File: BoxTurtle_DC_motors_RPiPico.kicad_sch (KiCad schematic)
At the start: 38 parts, among them J1 Power input, J10 DC motor 1, J11 DC motor 2, J12 DC motor 3, J13 DC motor 4, J14 Screw_Terminal_01x02, J15 CAN, J2 Power input, J3 Power output, J4 Power output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

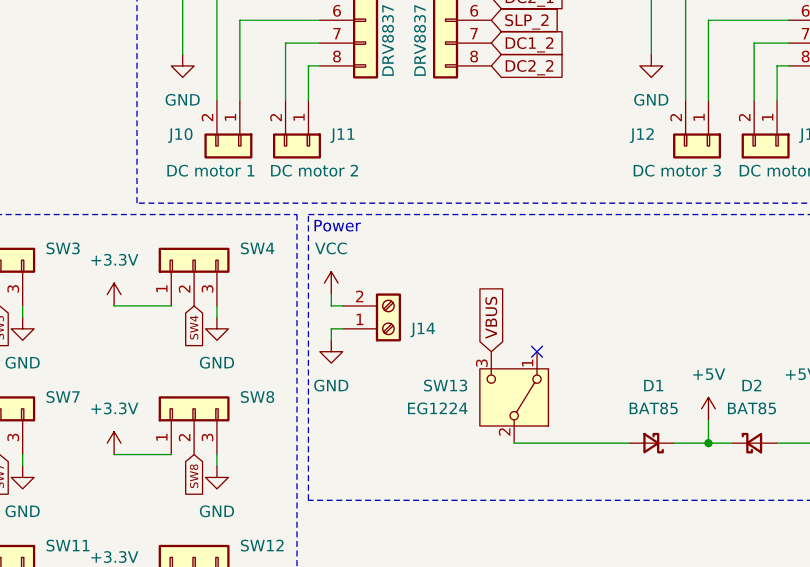
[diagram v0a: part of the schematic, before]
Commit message: Fuse & Gerber
Added the fuse for safety, also uploaded Gerber files for those who want to make their own board.
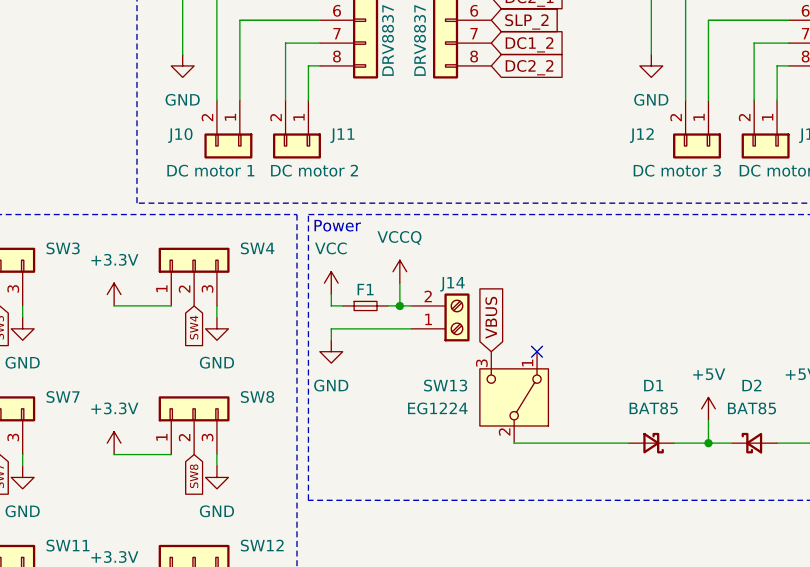
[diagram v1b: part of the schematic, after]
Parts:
- added F1: Fuse_Small, XF-506P:XF-506P, symbol Device:Fuse_Small
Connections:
- net VCC: now also F1.1; no longer J14.2 (Pin_2)
- new net VCCQ: F1.2, J14.2 (Pin_2)
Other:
- moved on the sheet: J14
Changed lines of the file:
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@@
 	)
 	(junction
+		(at 180.34 119.38)
+		(diameter 0)
+		(color 0 0 0 0)
+	)
+	(junction
 		(at 148.59 55.88)
 		(diameter 0)
@@
 	(wire
 		(pts
-			(xy 173.99 121.92) (xy 172.72 121.92)
+			(xy 172.72 121.92) (xy 181.61 121.92)
 		)
 		(stroke
@@
 	(wire
 		(pts
+			(xy 179.07 119.38) (xy 180.34 119.38)
+		)
+		(stroke
+			(width 0)
+			(type default)
+		)
+	)
+	(wire
+		(pts
 			(xy 214.63 132.08) (xy 214.63 134.62)
 		)
@@
 	(wire
 		(pts
+			(xy 180.34 116.84) (xy 180.34 119.38)
+		)
+		(stroke
+			(width 0)
+			(type default)
+		)
+	)
+	(wire
+		(pts
 			(xy 193.04 134.62) (xy 205.74 134.62)
 		)
@@
 	(wire
 		(pts
+			(xy 180.34 119.38) (xy 181.61 119.38)
+		)
+		(stroke
+			(width 0)
+			(type default)
+		)
+	)
+	(wire
+		(pts
 			(xy 138.43 119.38) (xy 138.43 120.65)
 		)
@@
 	)
 	(symbol
+		(lib_id "power:VCCQ")
+		(at 180.34 116.84 0)
+		(unit 1)
+		(exclude_from_sim no)
+		(in_bom yes)
+		(on_board yes)
+		(dnp no)
+		(fields_autoplaced yes)
+		(property "Reference" "#PWR053"
+			(at 180.34 120.65 0)
+			(effects
+				(font
+					(size 1.27 1.27)
+				)
+				(hide yes)
+			)
+		)
+		(property "Value" "VCCQ"
+			(at 180.34 111.76 0)
+			(effects
+				(font
+					(size 1.27 1.27)
+				)
+			)
+		)
+		(property "Footprint" ""
+			(at 180.34 116.84 0)
+			(effects
+				(font
+					(size 1.27 1.27)
+				)
+				(hide yes)
+			)
+		)
+		(property "Datasheet" ""
+			(at 180.34 116.84 0)
+			(effects
+				(font
+					(size 1.27 1.27)
+				)
+				(hide yes)
+			)
+		)
+		(property "Description" "Power symbol creates a global label with name \"VCCQ\""
+			(at 180.34 116.84 0)
+			(effects
+				(font
+					(size 1.27 1.27)
+				)
+				(hide yes)
+			)
+		)
+		(pin "1"
+		)
+		(instances
+			(project ""
+				(path "/1d127e4b-8316-4553-8f34-cd4a5b3a4711"
+					(reference "#PWR053")
+					(unit 1)
+				)
+			)
+		)
+	)
+	(symbol
 		(lib_id "power:GND")
 		(at 254 78.74 0)
@@
 	(symbol
 		(lib_id "Connector:Screw_Terminal_01x02")
-		(at 179.07 121.92 0)
+		(at 186.69 121.92 0)
 		(mirror x)
 		(unit 1)
@@
 		(dnp no)
 		(property "Reference" "J14"
-			(at 181.61 121.9201 0)
+			(at 184.912 116.84 0)
 			(effects
 				(font
@@
 		)
 		(property "Value" "Screw_Terminal_01x02"
-			(at 181.61 119.3801 0)
+			(at 189.23 119.3801 0)
 			(effects
 				(font
@@
 		)
 		(property "Footprint" "TerminalBlock_Phoenix:TerminalBlock_Phoenix_MKDS-3-2-5.08_1x02_P5.08mm_Horizontal"
-			(at 179.07 121.92 0)
+			(at 186.69 121.92 0)
 			(effects
 				(font
@@
 		)
 		(property "Datasheet" "~"
-			(at 179.07 121.92 0)
+			(at 186.69 121.92 0)
 			(effects
 				(font
@@
 		)
 		(property "Description" "Generic screw terminal, single row, 01x02, script generated (kicad-library-utils/schlib/autogen/connector/)"
-			(at 179.07 121.92 0)
+			(at 186.69 121.92 0)
 			(effects
 				(font
@@
 					(unit 1)
 				)
+			)
+		)
+	)
+	(symbol
+		(lib_id "Device:Fuse_Small")
+		(at 176.53 119.38 0)
+		(unit 1)
+		(exclude_from_sim no)
+		(in_bom yes)
+		(on_board yes)
+		(dnp no)
+		(property "Reference" "F1"
+			(at 176.53 117.602 0)
+			(effects
+				(font
+					(size 1.27 1.27)
+				)
+			)
+		)
+		(property "Value" "Fuse_Small"
+			(at 176.53 116.84 0)
+			(effects
+				(font
+					(size 1.27 1.27)
+				)
+				(hide yes)
+			)
+		)
+		(property "Footprint" "XF-506P:XF-506P"
+			(at 176.53 119.38 0)
+			(effects
+				(font
+					(size 1.27 1.27)
+				)
+				(hide yes)
+			)
+		)
+		(property "Datasheet" "~"
+			(at 176.53 119.38 0)
+			(effects
+				(font
+					(size 1.27 1.27)
+				)
+				(hide yes)
+			)
+		)
+		(property "Description" "Fuse, small symbol"
+			(at 176.53 119.38 0)
+			(effects
+				(font
+					(size 1.27 1.27)
+				)
+				(hide yes)
+			)
+		)
+		(pin "1"
+		)
+		(pin "2"
+		)
+		(instances
+			(project ""
+				(path "/1d127e4b-8316-4553-8f34-cd4a5b3a4711"
+					(reference "F1")
+					(unit 1)
+				)

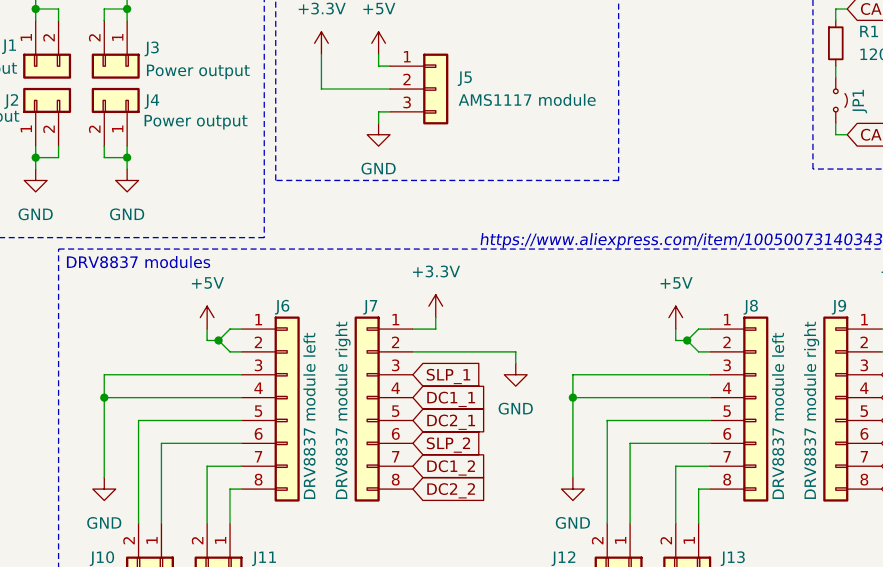
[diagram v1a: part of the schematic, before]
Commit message: Corrected 5V source for DC motors
As it was this board will blow your USB port.
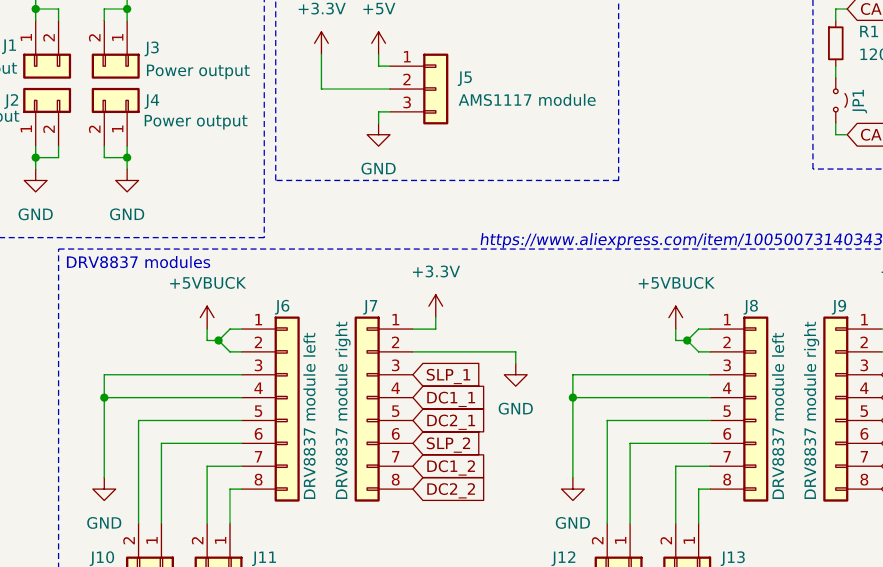
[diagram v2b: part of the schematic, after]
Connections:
- net +5V: no longer J6.1 (Pin_1), J6.2 (Pin_2), J8.1 (Pin_1), J8.2 (Pin_2)
- net +5VBUCK: now also J6.1 (Pin_1), J6.2 (Pin_2), J8.1 (Pin_1), J8.2 (Pin_2)
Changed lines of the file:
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@@
-	)
-	(symbol
-		(lib_id "power:+5V")
-		(at 219.71 74.93 0)
-		(unit 1)
-		(exclude_from_sim no)
-		(in_bom yes)
-		(on_board yes)
-		(dnp no)
-		(fields_autoplaced yes)
-		(property "Reference" "#PWR011"
-			(at 219.71 78.74 0)
-			(effects
-				(font
-					(size 1.27 1.27)
-				)
-				(hide yes)
-			)
-		)
-		(property "Value" "+5V"
-			(at 219.71 69.85 0)
-			(effects
-				(font
-					(size 1.27 1.27)
-				)
-			)
-		)
-		(property "Footprint" ""
-			(at 219.71 74.93 0)
-			(effects
-				(font
-					(size 1.27 1.27)
-				)
-				(hide yes)
-			)
-		)
-		(property "Datasheet" ""
-			(at 219.71 74.93 0)
-			(effects
-				(font
-					(size 1.27 1.27)
-				)
-				(hide yes)
-			)
-		)
-		(property "Description" "Power symbol creates a global label with name \"+5V\""
-			(at 219.71 74.93 0)
-			(effects
-				(font
-					(size 1.27 1.27)
-				)
-				(hide yes)
-			)
-		)
-		(pin "1"
-		)
-		(instances
-			(project "BoxTurtle_DC_motors_RPiPico"
-				(path "/1d127e4b-8316-4553-8f34-cd4a5b3a4711"
-					(reference "#PWR011")
-					(unit 1)
-				)
-			)
-		)
 	)
 	(symbol
@@
 	)
 	(symbol
+		(lib_id "power:+5VP")
+		(at 167.64 74.93 0)
+		(unit 1)
+		(exclude_from_sim no)
+		(in_bom yes)
+		(on_board yes)
+		(dnp no)
+		(fields_autoplaced yes)
+		(property "Reference" "#PWR054"
+			(at 167.64 78.74 0)
+			(effects
+				(font
+					(size 1.27 1.27)
+				)
+				(hide yes)
+			)
+		)
+		(property "Value" "+5VBUCK"
+			(at 167.64 69.85 0)
+			(effects
+				(font
+					(size 1.27 1.27)
+				)
+			)
+		)
+		(property "Footprint" ""
+			(at 167.64 74.93 0)
+			(effects
+				(font
+					(size 1.27 1.27)
+				)
+				(hide yes)
+			)
+		)
+		(property "Datasheet" ""
+			(at 167.64 74.93 0)
+			(effects
+				(font
+					(size 1.27 1.27)
+				)
+				(hide yes)
+			)
+		)
+		(property "Description" "Power symbol creates a global label with name \"+5VP\""
+			(at 167.64 74.93 0)
+			(effects
+				(font
+					(size 1.27 1.27)
+				)
+				(hide yes)
+			)
+		)
+		(pin "1"
+		)
+		(instances
+			(project "BoxTurtle_DC_motors_RPiPico"
+				(path "/1d127e4b-8316-4553-8f34-cd4a5b3a4711"
+					(reference "#PWR054")
+					(unit 1)
+				)
+			)
+		)
+	)
+	(symbol
 		(lib_id "Device:R_Small")
 		(at 237.49 43.18 0)
@@
 	)
 	(symbol
-		(lib_id "power:+5V")
-		(at 167.64 74.93 0)
-		(unit 1)
-		(exclude_from_sim no)
-		(in_bom yes)
-		(on_board yes)
-		(dnp no)
-		(fields_autoplaced yes)
-		(property "Reference" "#PWR010"
-			(at 167.64 78.74 0)
-			(effects
-				(font
-					(size 1.27 1.27)
-				)
-				(hide yes)
-			)
-		)
-		(property "Value" "+5V"
-			(at 167.64 69.85 0)
-			(effects
-				(font
-					(size 1.27 1.27)
-				)
-			)
-		)
-		(property "Footprint" ""
-			(at 167.64 74.93 0)
-			(effects
-				(font
-					(size 1.27 1.27)
-				)
-				(hide yes)
-			)
-		)
-		(property "Datasheet" ""
-			(at 167.64 74.93 0)
-			(effects
-				(font
-					(size 1.27 1.27)
-				)
-				(hide yes)
-			)
-		)
-		(property "Description" "Power symbol creates a global label with name \"+5V\""
-			(at 167.64 74.93 0)
-			(effects
-				(font
-					(size 1.27 1.27)
-				)
-				(hide yes)
-			)
-		)
-		(pin "1"
-		)
-		(instances
-			(project "BoxTurtle_DC_motors_RPiPico"
-				(path "/1d127e4b-8316-4553-8f34-cd4a5b3a4711"
-					(reference "#PWR010")
-					(unit 1)
-				)
-			)
-		)
-	)
-	(symbol
 		(lib_id "power:+3.3V")
 		(at 83.82 119.38 0)
@@
 					(unit 1)
 				)
+			)
+		)
+	)
+	(symbol
+		(lib_id "power:+5VP")
+		(at 219.71 74.93 0)
+		(unit 1)
+		(exclude_from_sim no)
+		(in_bom yes)
+		(on_board yes)
+		(dnp no)
+		(fields_autoplaced yes)
+		(property "Reference" "#PWR055"
+			(at 219.71 78.74 0)
+			(effects
+				(font
+					(size 1.27 1.27)
+				)
+				(hide yes)
+			)
+		)
+		(property "Value" "+5VBUCK"
+			(at 219.71 69.85 0)
+			(effects
+				(font
+					(size 1.27 1.27)
+				)
+			)
+		)
+		(property "Footprint" ""
+			(at 219.71 74.93 0)
+			(effects
+				(font
+					(size 1.27 1.27)
+				)
+				(hide yes)
+			)
+		)
+		(property "Datasheet" ""
+			(at 219.71 74.93 0)
+			(effects
+				(font
+					(size 1.27 1.27)
+				)
+				(hide yes)
+			)
+		)
+		(property "Description" "Power symbol creates a global label with name \"+5VP\""
+			(at 219.71 74.93 0)
+			(effects
+				(font
+					(size 1.27 1.27)
+				)
+				(hide yes)
+			)
+		)
+		(pin "1"
+		)
+		(instances
+			(project "BoxTurtle_DC_motors_RPiPico"
+				(path "/1d127e4b-8316-4553-8f34-cd4a5b3a4711"
+					(reference "#PWR055")
+					(unit 1)
+				)

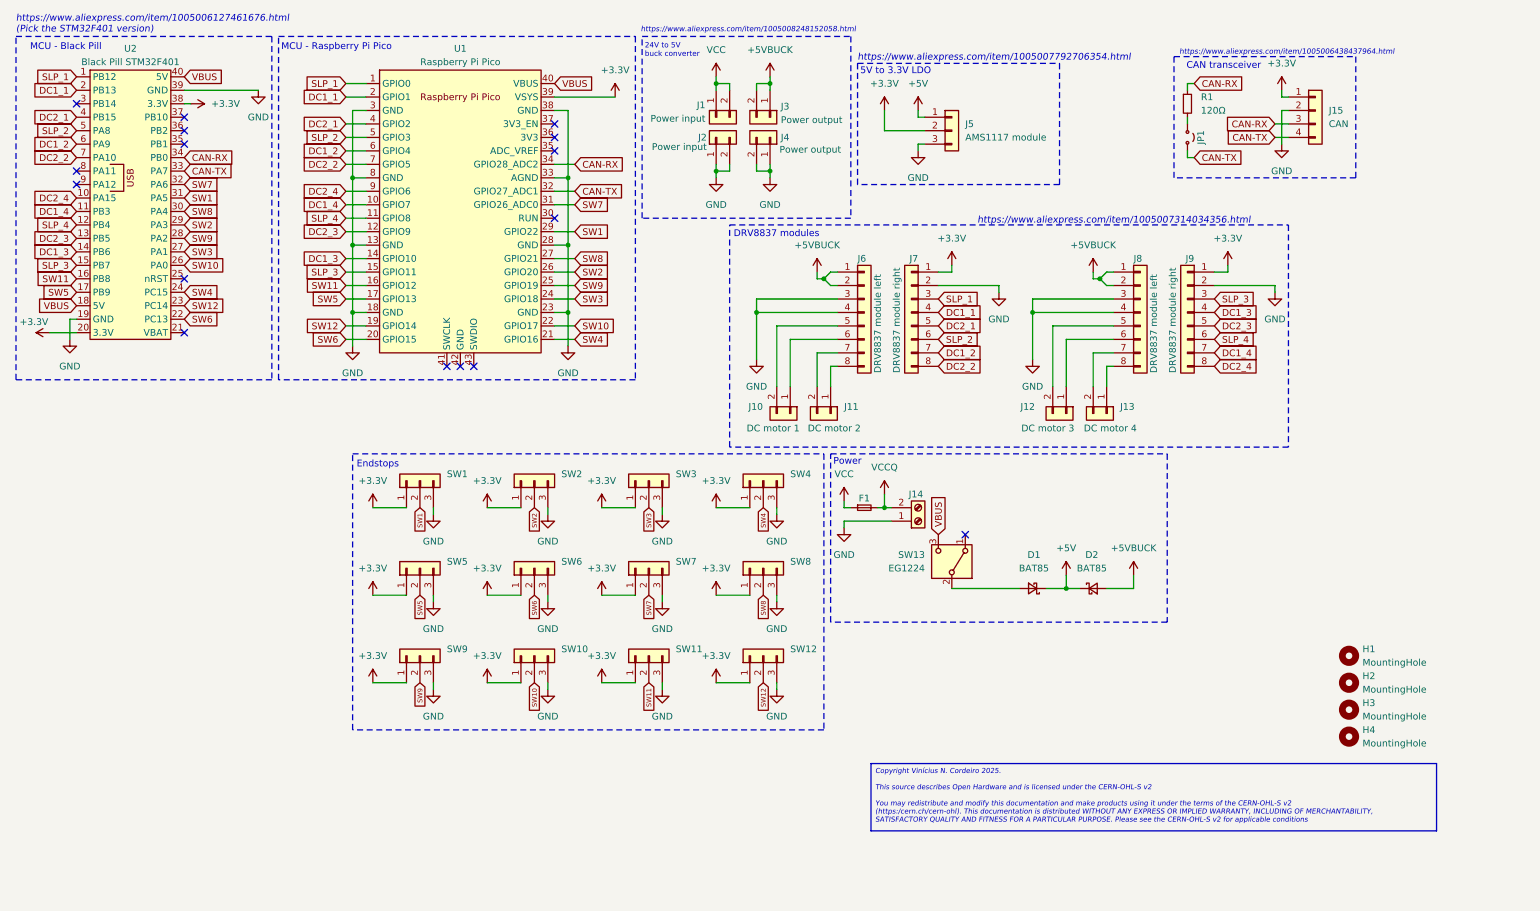
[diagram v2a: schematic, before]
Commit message: Revision 2.4 - QoL updates
Increased CAN bus resistor footprint; reduced hole diameter on Raspberry Pi Pico's socket pads for snugger fit; changed pin for SW6 on the Black Pill.
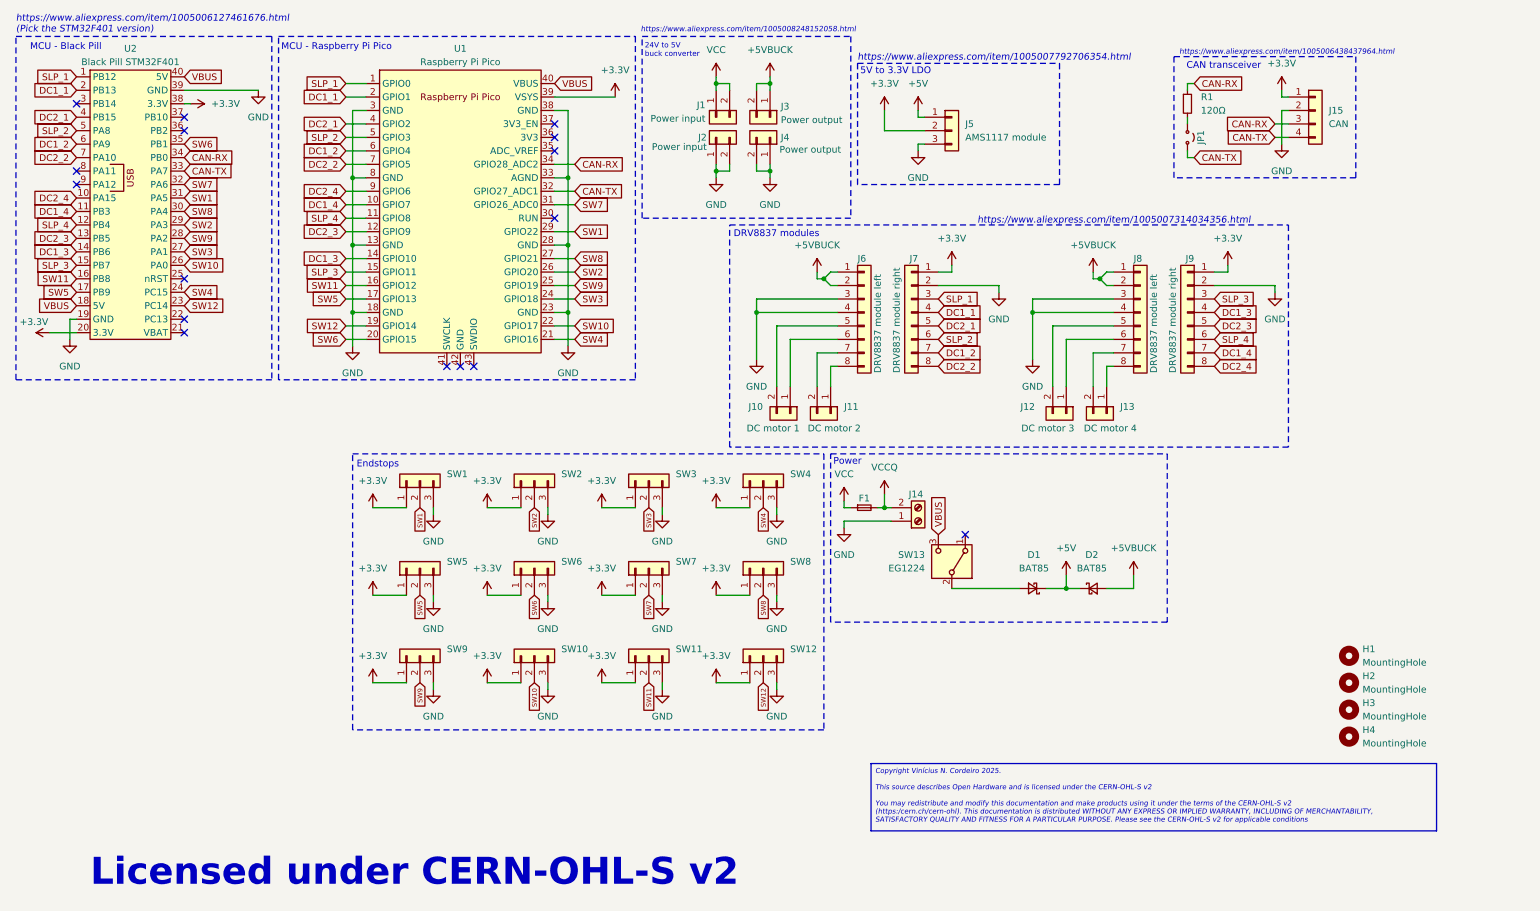
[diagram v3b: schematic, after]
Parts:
- R1: footprint Resistor_THT:R_Axial_DIN0204_L3.6mm_D1.6mm_P7.62mm_Horizontal -> Resistor_THT:R_Axial_DIN0207_L6.3mm_D2.5mm_P10.16mm_Horizontal
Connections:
- net SW6: now also U2.35 (PB1); no longer U2.22 (PC13)
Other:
- note added: "Licensed under CERN-OHL-S v2"
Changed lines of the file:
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@@
 	(title_block
 		(title "BoxTurtle DC motors standalone board")
-		(date "2025-02-03")
-		(rev "2.1")
+		(date "2025-02-22")
+		(rev "2.4")
 	)
 	(junction
@@
 	)
 	(no_connect
-		(at 48.26 50.8)
+		(at 48.26 83.82)
 	)
 	(no_connect
@@
 		)
 	)
+	(text "Licensed under CERN-OHL-S v2"
+		(exclude_from_sim no)
+		(at 91.694 188.214 0)
+		(effects
+			(font
+				(size 5.08 5.08)
+				(thickness 1.016)
+				(bold yes)
+			)
+		)
+	)
 	(text "https://www.aliexpress.com/item/1005006438437964.html"
 		(exclude_from_sim no)
@@
 	(global_label "SW6"
 		(shape input)
-		(at 48.26 83.82 0)
+		(at 48.26 50.8 0)
 		(fields_autoplaced yes)
 		(effects
@@
 		)
 		(property "Intersheetrefs" "${INTERSHEET_REFS}"
-			(at 55.1156 83.82 0)
+			(at 55.1156 50.8 0)
 			(effects
 				(font
@@
 			)
 		)
-		(property "Footprint" "Resistor_THT:R_Axial_DIN0204_L3.6mm_D1.6mm_P7.62mm_Horizontal"
+		(property "Footprint" "Resistor_THT:R_Axial_DIN0207_L6.3mm_D2.5mm_P10.16mm_Horizontal"
 			(at 237.49 43.18 0)
 			(effects

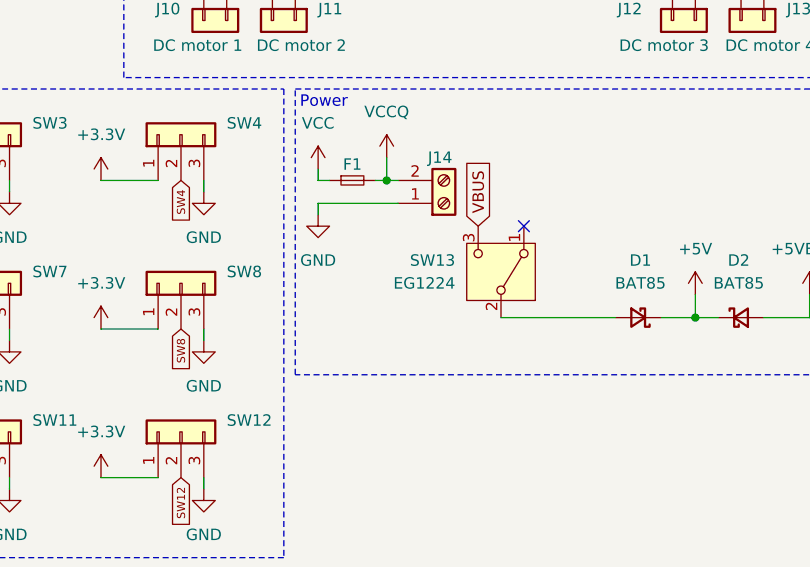
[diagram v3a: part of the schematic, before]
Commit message: Revision 2.6
Updated footprints again now that I have them on hand to accurately make measures, changed selection switch for a model that is smaller and carry more current.
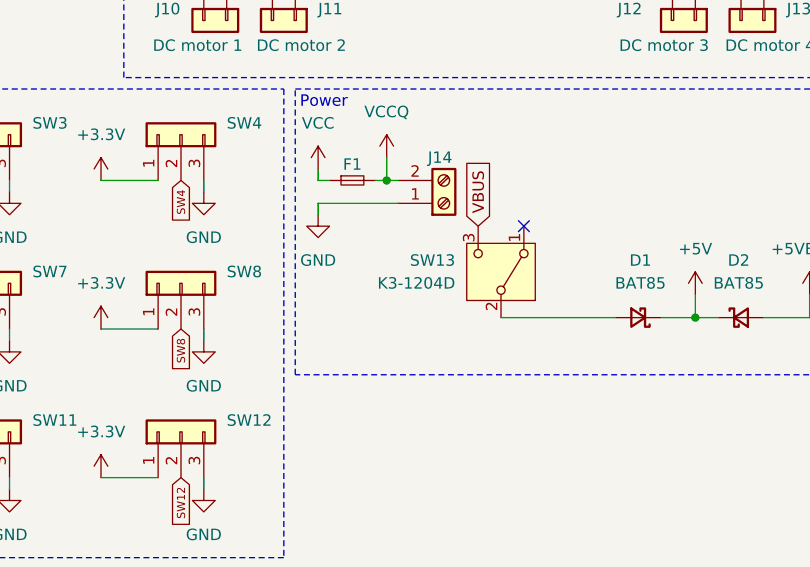
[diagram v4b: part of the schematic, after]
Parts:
- SW13: value EG1224 -> K3-1204D; footprint Button_Switch_THT:SW_E-Switch_EG1224_SPDT_Angled -> K3-1204D:K3-1204D
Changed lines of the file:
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@@
 			)
 		)
-		(property "Value" "EG1224"
+		(property "Value" "K3-1204D"
 			(at 187.96 130.8099 90)
 			(effects
@@
 			)
 		)
-		(property "Footprint" "Button_Switch_THT:SW_E-Switch_EG1224_SPDT_Angled"
+		(property "Footprint" "K3-1204D:K3-1204D"
 			(at 193.04 129.54 0)
 			(effects
